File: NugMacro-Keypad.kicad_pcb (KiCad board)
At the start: 2 copper layers, 76.2 x 97.2 mm, 51 parts, among them J2 Conn_01x04, J3 Conn_01x04_Female_For_LCD, SW1 SW_Push, SW2 RotaryEncoder_Switch, U1 ATmega32U4-A, Y1 16MHz

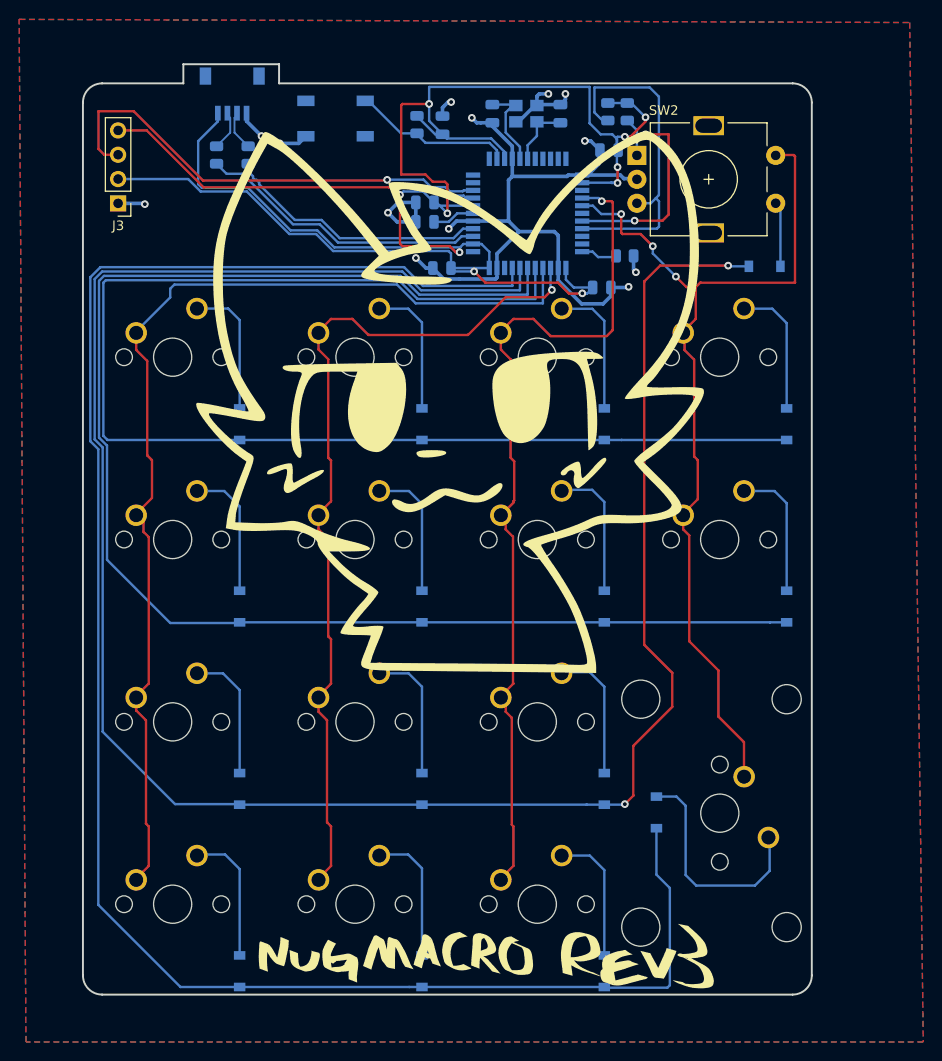
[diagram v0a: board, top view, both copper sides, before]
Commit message: Second Version of Rev3 ig?
fixed wiring on oled, made 1.5u key look a bit better, pulled back the jst connector to hopefully make  compatible for a rubber o ring gasket mount.
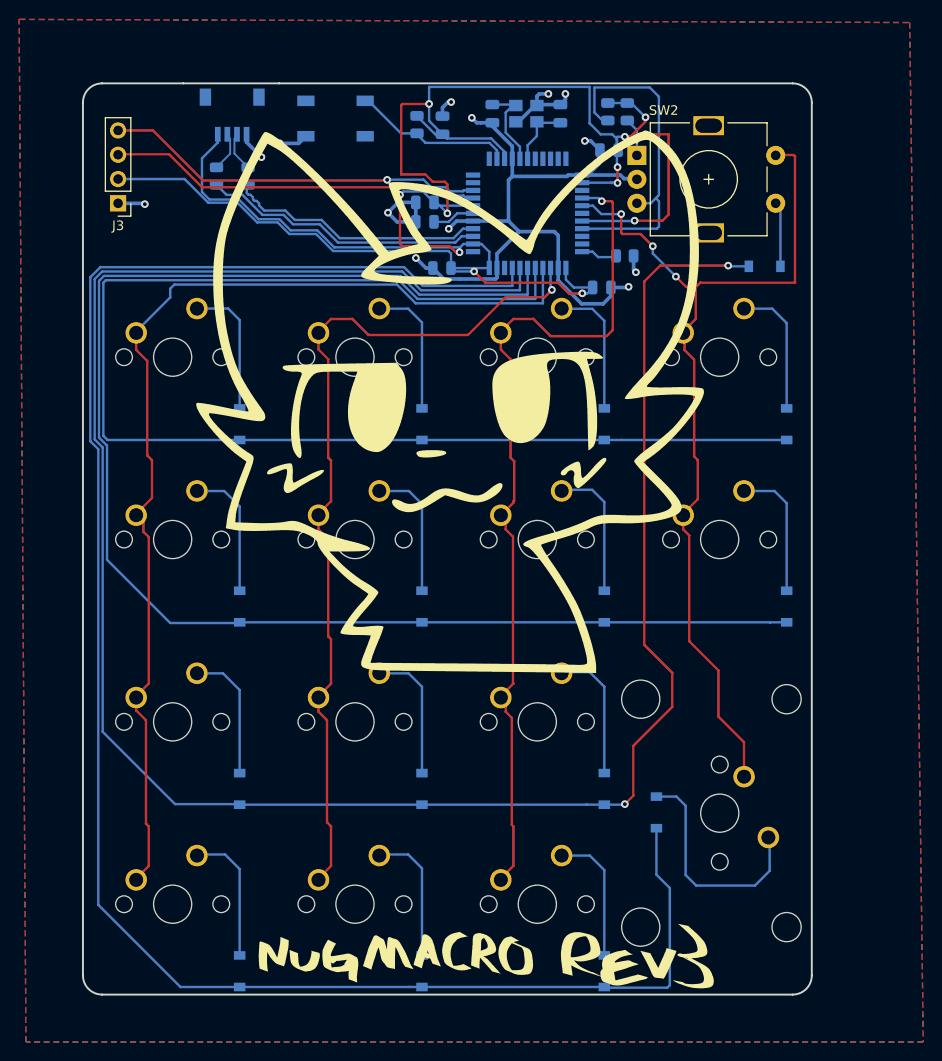
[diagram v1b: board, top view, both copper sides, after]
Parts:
- moved J2 2.20 mm to (120.1, 45.6)
- moved R2 2.20 mm to (118.5, 54.7)
- moved R3 2.20 mm to (121.8, 54.7)
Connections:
- U1 pad 8: OLED1 -> OLED2
- U1 pad 9: OLED2 -> OLED1
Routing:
- net OLED2: track 48.9 -> 39.1 mm
- net +5V: track 208.5 -> 206.2 mm
- net Net-(R2-Pad1): track 30.5 -> 29.6 mm
- net Net-(R3-Pad1): track 28.0 -> 27.1 mm
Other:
- board size 76.2 x 97.2 mm -> 76.2 x 95.2 mm
